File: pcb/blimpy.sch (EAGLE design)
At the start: 42 parts, among them IC1 TB6612FNG, J2 MICRO-USB, J3 JSTPH, Q1 mmbt2222, Q2 mmbt2222, Q3 DMG3415U, U1 RGB, U2 AP2112-3.3, U3 MCP73831T-2, U4 BNO080, U7 CP2104, U9 ESP-WROOM-32

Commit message: updated board design
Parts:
- removed C11: 10uF, SparkFun-Capacitors:10UF-0603-6.3V-20%
- removed IC1: TB6612FNG, adafruit:TB6612FNG
- added C12, C14, C15, C16, C17, C18, C19, C21, C22, C24, C25, C27: 0.1uF, SparkFun-Capacitors:0.1UF-0603-25V-5%
- added C28, C29, C30, C31: 10uF, SparkFun-Capacitors:10UF-POLAR-EIA3216-16V-10%(TANT)
- added C9: 10uF, SparkFun-Capacitors:10UF-0603-6.3V-20%
- added CN1, CN2, CN3, CN4, CN5, CN6, CN7, CN8: (no value), adafruit:JST_2PIN-SMT-RA
- added HB1, HB2, HB3, HB4: TB6612FNG, adafruit:TB6612FNG
- added J1: JSTPH, microbuilder:CON_JST_PH_2PIN
- added U5, U6: SX1509, SparkFun-IC-Special-Function:SX1509
- R4: value 4.7k -> 2.0k; device SparkFun-Resistors:4.7KOHM-0603-1/10W-1% -> SparkFun-Resistors:2.0KOHM-0603-1/10W-5%
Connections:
- removed net N$20: IC1.AO2, IC1.AO2'
- removed net N$24: IC1.BO1, IC1.BO1'
- removed net VBAT: C11.1, C3.1, C5.1, IC1.VM1, IC1.VM2, IC1.VM3, J3.2, Q3.D, R1.2, U3.VBAT
- removed net VBUS: D1.A, D2.A, J2.VBUS, Q3.G, R12.2, U3.VDD, U7G$1.VBUS
- new net IO1_RST: U5.!RESET
- new net IO2_RST: U6.!RESET
- new net M1_DIR: U5.I/O[12], U6.I/O[12]
- new net M1_PWM: U5.I/O[13], U6.I/O[13]
- new net M2_DIR: U5.I/O[14], U6.I/O[14]
- new net M2_PWM: U5.I/O[15], U6.I/O[15]
- new net M3_DIR: U5.I/O[8], U6.I/O[8]
- new net M3_PWM: U5.I/O[9], U6.I/O[9]
- new net M4_DIR: U5.I/O[10], U6.I/O[10]
- new net M4_PWM: U5.I/O[11], U6.I/O[11]
- new net M5_DIR: U5.I/O[4], U6.I/O[4]
- new net M5_PWM: U5.I/O[5], U6.I/O[5]
- new net M6_DIR: U5.I/O[6], U6.I/O[6]
- new net M6_PWM: U5.I/O[7], U6.I/O[7]
- new net N$17: CN1.1, HB1.AO2, HB1.AO2'
- new net N$21: CN2.1, HB1.BO1, HB1.BO1'
- new net N$23: CN3.2, HB2.AO1, HB2.AO1'
- new net N$25: CN3.1, HB2.AO2, HB2.AO2'
- new net N$33: CN4.1, HB2.BO1, HB2.BO1'
- new net N$35: CN5.1, HB3.AO2, HB3.AO2'
- new net N$37: CN6.1, HB3.BO1, HB3.BO1'
- new net N$38: CN7.2, HB4.AO1, HB4.AO1'
- new net N$39: CN7.1, HB4.AO2, HB4.AO2'
- new net N$41: CN8.1, HB4.BO1, HB4.BO1'
- new net N$5: CN1.2, HB1.AO1, HB1.AO1'
- new net S1_SIG: U5.I/O[0], U6.I/O[0]
- new net S2_SIG: U5.I/O[1], U6.I/O[1]
- new net S3_SIG: U5.I/O[2], U6.I/O[2]
- new net S4_SIG: U5.I/O[3], U6.I/O[3]
- new net V_BATT: C19.1, C22.1, C25.1, C28.+, C29.+, C3.1, C30.+, C31.+, C5.1, HB1.VM1, HB1.VM2, HB1.VM3, HB2.VM1, HB2.VM2, HB2.VM3, HB3.VM1, HB3.VM2, HB3.VM3, HB4.VM1, HB4.VM2, HB4.VM3, J3.2, Q3.D, R1.2, U3.VBAT
- new net V_USB: C9.1, D1.A, D2.A, J2.VBUS, Q3.G, R12.2, U3.VDD, U7G$1.VBUS
- net 3.3V: now also C12.1, C14.1, C15.1, C16.1, C17.1, C18.1, C21.1, C24.1, C27.1, HB1.STBY, HB1.VCC, HB2.STBY, HB2.VCC, HB3.STBY, HB3.VCC, HB4.STBY, HB4.VCC, U5.VCC1, U5.VCC2, U5.VDDM, U6.ADDR0, U6.VCC1, U6.VCC2, U6.VDDM; no longer IC1.STBY, IC1.VCC
- net GND: now also C12.2, C14.2, C15.2, C16.2, C17.2, C18.2, C19.2, C21.2, C22.2, C24.2, C25.2, C27.2, C28.-, C29.-, C30.-, C31.-, C9.2, HB1.GND, HB1.PGND1, HB1.PGND1', HB1.PGND2, HB1.PGND2', HB2.GND, HB2.PGND1, HB2.PGND1', HB2.PGND2, HB2.PGND2', HB3.GND, HB3.PGND1, HB3.PGND1', HB3.PGND2, HB3.PGND2', HB4.GND, HB4.PGND1, HB4.PGND1', HB4.PGND2, HB4.PGND2', U5.ADDR0, U5.ADDR1, U5.GND, U6.ADDR1, U6.GND; no longer C11.2, IC1.GND, IC1.PGND1, IC1.PGND1', IC1.PGND2, IC1.PGND2'
- net N$18: now also CN5.2, HB3.AO1, HB3.AO1'; no longer IC1.AO1, IC1.AO1'
- net N$22: now also CN2.2, CN4.2, CN6.2, CN8.2, HB1.BO2, HB1.BO2', HB2.BO2, HB2.BO2', HB3.BO2, HB3.BO2', HB4.BO2, HB4.BO2'; no longer IC1.BO2, IC1.BO2'
- net N$26: now also HB1.PWMB, HB2.PWMB, HB3.PWMB, HB4.PWMB; no longer IC1.PWMB
- net N$27: now also HB1.BIN2, HB2.BIN2, HB3.BIN2, HB4.BIN2; no longer IC1.BIN2
- net N$28: now also HB1.BIN1, HB2.BIN1, HB3.BIN1, HB4.BIN1; no longer IC1.BIN1
- net N$30: now also HB1.AIN1, HB2.AIN1, HB3.AIN1, HB4.AIN1; no longer IC1.AIN1
- net N$31: now also HB1.AIN2, HB2.AIN2, HB3.AIN2, HB4.AIN2; no longer IC1.AIN2
- net N$32: now also HB1.PWMA, HB2.PWMA, HB3.PWMA, HB4.PWMA; no longer IC1.PWMA
- net SCL: now also U5.SCL, U6.SCL
- net SDA: now also U5.SDA, U6.SDA
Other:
- note added: "600mA (800mA max)"
- note added: "GPIO Expander 1 I2C Address: 0x3E"
- note added: "GPIO Expander 2 I2C Address: 0x3F"
- note added: "TODO - Connect IMU to MC - Connect IO1 and IO2 to MC - Servos - H-Bridges - Add. Battery - Expose unused GPIO - ESD Protection? - Capacitors"
- note added: "up to 500mA charging current"
- note removed: "up to 200mA charging current"
- moved on the sheet: C1, C10, C13, C2, C3, C4, C5, C6, C7, C8, D1, D2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

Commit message: updated
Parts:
- removed CN1, CN2, CN3, CN4, CN5, CN6, CN7, CN8: (no value), adafruit:JST_2PIN-SMT-RA
- removed J3: JSTPH, microbuilder:CON_JST_PH_2PIN
- added J10, J11, J12, J13, J14, J15, J8, J9: (no value), SparkFun-Connectors:CONN_02-JST-2MM-SMT
- added J4, J5, J6, J7: 3-PIN SMD, SparkFun-Connectors:CONN_03JST-SMD
- added JP1: JUMPER-SMT_2_NO_SILK, SparkFun-Jumpers:JUMPER-SMT_2_NO_SILK
- J1: value JSTPH -> MICRO-USB; device microbuilder:CON_JST_PH_2PIN -> SparkFun-Connectors:USB_MICRO-B_SMT
- J2: value MICRO-USB -> (none); device SparkFun-Connectors:USB_MICRO-B_SMT -> SparkFun-Connectors:CONN_02-JST-2MM-SMT
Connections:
- removed net M1_DIR: U5.I/O[12], U6.I/O[12]
- removed net M1_PWM: U5.I/O[13], U6.I/O[13]
- removed net M2_DIR: U5.I/O[14], U6.I/O[14]
- removed net M2_PWM: U5.I/O[15], U6.I/O[15]
- removed net M3_DIR: U5.I/O[8], U6.I/O[8]
- removed net M3_PWM: U5.I/O[9], U6.I/O[9]
- removed net M4_DIR: U5.I/O[10], U6.I/O[10]
- removed net M4_PWM: U5.I/O[11], U6.I/O[11]
- removed net M5_DIR: U5.I/O[4], U6.I/O[4]
- removed net M5_PWM: U5.I/O[5], U6.I/O[5]
- removed net M6_DIR: U5.I/O[6], U6.I/O[6]
- removed net M6_PWM: U5.I/O[7], U6.I/O[7]
- removed net N$26: HB1.PWMB, HB2.PWMB, HB3.PWMB, HB4.PWMB
- removed net N$27: HB1.BIN2, HB2.BIN2, HB3.BIN2, HB4.BIN2
- removed net N$28: HB1.BIN1, HB2.BIN1, HB3.BIN1, HB4.BIN1
- removed net N$30: HB1.AIN1, HB2.AIN1, HB3.AIN1, HB4.AIN1
- removed net N$31: HB1.AIN2, HB2.AIN2, HB3.AIN2, HB4.AIN2
- removed net N$32: HB1.PWMA, HB2.PWMA, HB3.PWMA, HB4.PWMA
- removed net S1_SIG: U5.I/O[0], U6.I/O[0]
- removed net S2_SIG: U5.I/O[1], U6.I/O[1]
- removed net S3_SIG: U5.I/O[2], U6.I/O[2]
- removed net S4_SIG: U5.I/O[3], U6.I/O[3]
- new net 1-1: U5.I/O[0]
- new net 1-10: U5.I/O[9]
- new net 1-11: U5.I/O[10]
- new net 1-12: U5.I/O[11]
- new net 1-13: U5.I/O[12]
- new net 1-14: U5.I/O[13]
- new net 1-15: U5.I/O[14]
- new net 1-16: U5.I/O[15]
- new net 1-2: U5.I/O[1]
- new net 1-3: U5.I/O[2]
- new net 1-4: U5.I/O[3]
- new net 1-5: U5.I/O[4]
- new net 1-6: U5.I/O[5]
- new net 1-7: U5.I/O[6]
- new net 1-8: U5.I/O[7]
- new net 1-9: U5.I/O[8]
- new net 2-1: U6.I/O[0]
- new net 2-10: U6.I/O[9]
- new net 2-11: U6.I/O[10]
- new net 2-12: U6.I/O[11]
- new net 2-13: U6.I/O[12]
- new net 2-14: U6.I/O[13]
- new net 2-15: U6.I/O[14]
- new net 2-16: U6.I/O[15]
- new net 2-2: U6.I/O[1]
- new net 2-3: U6.I/O[2]
- new net 2-4: U6.I/O[3]
- new net 2-5: U6.I/O[4]
- new net 2-6: U6.I/O[5]
- new net 2-7: U6.I/O[6]
- new net 2-8: U6.I/O[7]
- new net 2-9: U6.I/O[8]
- new net H1-1: HB1.PWMA
- new net H1-2: HB1.AIN2
- new net H1-3: HB1.AIN1
- new net H1-4: HB1.BIN1
- new net H1-5: HB1.BIN2
- new net H1-6: HB1.PWMB
- new net H2-1: HB2.PWMA
- new net H2-2: HB2.AIN2
- new net H2-3: HB2.AIN1
- new net H2-4: HB2.BIN1
- new net H2-5: HB2.BIN2
- new net H2-6: HB2.PWMB
- new net H3-1: HB3.PWMA
- new net H3-2: HB3.AIN2
- new net H3-3: HB3.AIN1
- new net H3-4: HB3.BIN1
- new net H3-5: HB3.BIN2
- new net H3-6: HB3.PWMB
- new net H4-1: HB4.PWMA
- new net H4-2: HB4.AIN2
- new net H4-3: HB4.AIN1
- new net H4-4: HB4.BIN1
- new net H4-5: HB4.BIN2
- new net H4-6: HB4.PWMB
- new net N$19: J4.3, J5.3, J6.3, J7.3
- net GND: now also J1.GND, J1.SHIELD, J2.2, J4.2, J5.2, J6.2, J7.2; no longer J2.GND, J2.SHIELD, J3.1
- net N$17: now also J8.1; no longer CN1.1
- net N$18: now also J12.2; no longer CN5.2
- net N$2: now also J1.D+; no longer J2.D+
- net N$21: now also J9.1; no longer CN2.1
- net N$22: now also J11.2, J13.2, J15.2, J9.2; no longer CN2.2, CN4.2, CN6.2, CN8.2
- net N$23: now also J10.2; no longer CN3.2
- net N$25: now also J10.1; no longer CN3.1
- net N$33: now also J11.1; no longer CN4.1
- net N$35: now also J12.1; no longer CN5.1
- net N$37: now also J13.1; no longer CN6.1
- net N$38: now also J14.2; no longer CN7.2
- net N$39: now also J14.1; no longer CN7.1
- net N$4: now also JP1.1
- net N$41: now also J15.1; no longer CN8.1
- net N$5: now also J8.2; no longer CN1.2
- net N$6: now also J1.D-; no longer J2.D-
- net V_BATT: now also J2.1, J4.1, J5.1, J6.1, J7.1; no longer J3.2
- net V_USB: now also J1.VBUS, JP1.2; no longer J2.VBUS
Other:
- note added: "BOARD POWER"
- note added: "MOTORS"
- note added: "SERVOS"
- note added: "TODO - Connect IMU to MC - Connect Servos to MC - Connect H-Bridges to IOs - Connect IOs to MC - Expose unused GPIOs - ESD Protection? - Capacitors - Check all components"
- note added: "up to 500mA charging current close jumper to disable"
- note removed: "POWER AND FILTERING"
- note removed: "TODO - Connect IMU to MC - Connect IO1 and IO2 to MC - Servos - H-Bridges - Add. Battery - Expose unused GPIO - ESD Protection? - Capacitors"
- note removed: "up to 500mA charging current"
- moved on the sheet: C13, C19, C21, C22, C24, C25, C27, C28, C29, C30, C31, C5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

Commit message: added battery gauge
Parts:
- removed R1, R3: 100k, SparkFun-Resistors:100KOHM-0603-1/10W-1%
- added C11: 0.1uF, SparkFun-Capacitors:0.1UF-0603-25V-5%
- added U10: MAX17048, SparkFun-IC-Power:MAX17048DFN8
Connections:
- removed net BAT: R1.1, R3.2, U9.34-IA
- net GND: now also C11.2, U10.CTG, U10.GND, U10.QSTRT; no longer R3.1
- net SCL: now also U10.SCL
- net SDA: now also U10.SDA
- net V_BATT: now also C11.1, U10.CELL, U10.VDD; no longer R1.2
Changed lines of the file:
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@@
 <part name="Q3" library="microbuilder" deviceset="MOSFET-P" device="" value="DMG3415U"/>
 <part name="R12" library="SparkFun-Resistors" deviceset="100KOHM" device="-0603-1/10W-1%" value="100k"/>
-<part name="R1" library="SparkFun-Resistors" deviceset="100KOHM" device="-0603-1/10W-1%" value="100k"/>
-<part name="R3" library="SparkFun-Resistors" deviceset="100KOHM" device="-0603-1/10W-1%" value="100k"/>
 <part name="R4" library="SparkFun-Resistors" library_urn="urn:adsk.eagle:library:532" deviceset="2.0KOHM" device="-0603-1/10W-5%" package3d_urn="urn:adsk.eagle:package:39650/1" value="2.0k"/>
 <part name="S1" library="SparkFun-Switches" deviceset="SWITCH-SPDT" device="-SMD-RIGHT-ANGLE" value="PWR"/>
@@
 <part name="J7" library="SparkFun-Connectors" library_urn="urn:adsk.eagle:library:513" deviceset="CONN_03" device="JST-SMD" package3d_urn="urn:adsk.eagle:package:38075/1" value="3-PIN SMD"/>
 <part name="JP1" library="SparkFun-Jumpers" library_urn="urn:adsk.eagle:library:528" deviceset="JUMPER-SMT_2_NO" device="_SILK" package3d_urn="urn:adsk.eagle:package:39279/1"/>
+<part name="U10" library="SparkFun-IC-Power" library_urn="urn:adsk.eagle:library:526" deviceset="MAX17048" device="DFN8" package3d_urn="urn:adsk.eagle:package:39085/1" value="MAX17048"/>
+<part name="C11" library="SparkFun-Capacitors" library_urn="urn:adsk.eagle:library:510" deviceset="0.1UF" device="-0603-25V-5%" package3d_urn="urn:adsk.eagle:package:37414/1" value="0.1uF"/>
 </parts>
 <sheets>
@@
 <text x="200.66" y="124.46" size="1.778" layer="94">PROGRAMMING</text>
 <text x="17.78" y="121.92" size="1.27" layer="97">CHARGING LED</text>
-<text x="93.98" y="121.92" size="1.27" layer="97">CHARGE
+<text x="121.92" y="127" size="1.27" layer="97">CHARGE
 MEASUREMENT</text>
 <text x="43.18" y="45.72" size="1.778" layer="94">I2C PULL-UP
@@
 I2C Address: 0x4A</text>
 <text x="378.46" y="185.42" size="1.27" layer="97">INT OSC</text>
-<text x="665.48" y="220.98" size="5.08" layer="94" align="top-left">TODO
+<text x="160.02" y="-58.42" size="5.08" layer="94" align="top-left">TODO
 - Connect IMU to MC
 - Connect Servos to MC
@@
 <attribute name="VALUE" x="29.464" y="182.88" size="1.778" layer="96" font="vector" rot="R90" align="top-center"/>
 </instance>
-<instance part="R1" gate="G$1" x="106.68" y="111.76" smashed="yes" rot="R90">
-<attribute name="NAME" x="105.156" y="111.76" size="1.778" layer="95" font="vector" rot="R90" align="bottom-center"/>
-<attribute name="VALUE" x="108.204" y="111.76" size="1.778" layer="96" font="vector" rot="R90" align="top-center"/>
-</instance>
-<instance part="R3" gate="G$1" x="106.68" y="96.52" smashed="yes" rot="R90">
-<attribute name="NAME" x="105.156" y="96.52" size="1.778" layer="95" font="vector" rot="R90" align="bottom-center"/>
-<attribute name="VALUE" x="108.204" y="96.52" size="1.778" layer="96" font="vector" rot="R90" align="top-center"/>
-</instance>
 <instance part="R4" gate="G$1" x="78.74" y="106.68" smashed="yes" rot="R90">
 <attribute name="NAME" x="77.216" y="106.68" size="1.778" layer="95" font="vector" rot="R90" align="bottom-center"/>
@@
 <instance part="JP1" gate="G$1" x="78.74" y="127" smashed="yes" rot="R90">
 <attribute name="NAME" x="76.2" y="124.46" size="1.778" layer="95" font="vector" rot="R90"/>
+</instance>
+<instance part="U10" gate="G$1" x="132.08" y="111.76" smashed="yes">
+<attribute name="NAME" x="121.92" y="122.428" size="1.778" layer="95" font="vector"/>
+<attribute name="VALUE" x="121.92" y="99.06" size="1.778" layer="96" font="vector"/>
+</instance>
+<instance part="C11" gate="G$1" x="106.68" y="106.68" smashed="yes">
+<attribute name="NAME" x="108.204" y="109.601" size="1.778" layer="95" font="vector"/>
+<attribute name="VALUE" x="108.204" y="104.521" size="1.778" layer="96" font="vector"/>
 </instance>
 </instances>
@@
 </segment>
 <segment>
-<pinref part="R3" gate="G$1" pin="1"/>
 <pinref part="U3" gate="G$1" pin="VSS"/>
-<wire x1="106.68" y1="88.9" x2="106.68" y2="91.44" width="0.1524" layer="91"/>
 <wire x1="68.58" y1="114.3" x2="71.12" y2="114.3" width="0.1524" layer="91"/>
 <wire x1="71.12" y1="114.3" x2="71.12" y2="96.52" width="0.1524" layer="91"/>
@@
 <wire x1="35.56" y1="96.52" x2="71.12" y2="96.52" width="0.1524" layer="91"/>
 <junction x="71.12" y="96.52"/>
-<wire x1="106.68" y1="88.9" x2="88.9" y2="88.9" width="0.1524" layer="91"/>
-<wire x1="88.9" y1="88.9" x2="88.9" y2="96.52" width="0.1524" layer="91"/>
-<junction x="88.9" y="96.52"/>
 <wire x1="78.74" y1="101.6" x2="78.74" y2="96.52" width="0.1524" layer="91"/>
 <junction x="78.74" y="96.52"/>
 <pinref part="GND12" gate="1" pin="GND"/>
 <wire x1="71.12" y1="88.9" x2="71.12" y2="96.52" width="0.1524" layer="91"/>
+<pinref part="U10" gate="G$1" pin="QSTRT"/>
+<wire x1="142.24" y1="104.14" x2="144.78" y2="104.14" width="0.1524" layer="91"/>
+<wire x1="144.78" y1="104.14" x2="144.78" y2="96.52" width="0.1524" layer="91"/>
+<pinref part="U10" gate="G$1" pin="CTG"/>
+<wire x1="119.38" y1="109.22" x2="116.84" y2="109.22" width="0.1524" layer="91"/>
+<pinref part="U10" gate="G$1" pin="GND"/>
+<wire x1="119.38" y1="104.14" x2="116.84" y2="104.14" width="0.1524" layer="91"/>
+<wire x1="116.84" y1="109.22" x2="116.84" y2="104.14" width="0.1524" layer="91"/>
+<wire x1="116.84" y1="104.14" x2="116.84" y2="96.52" width="0.1524" layer="91"/>
+<junction x="116.84" y="104.14"/>
+<wire x1="144.78" y1="96.52" x2="116.84" y2="96.52" width="0.1524" layer="91"/>
+<junction x="116.84" y="96.52"/>
+<wire x1="88.9" y1="96.52" x2="106.68" y2="96.52" width="0.1524" layer="91"/>
+<junction x="88.9" y="96.52"/>
+<pinref part="C11" gate="G$1" pin="2"/>
+<wire x1="106.68" y1="96.52" x2="116.84" y2="96.52" width="0.1524" layer="91"/>
+<wire x1="106.68" y1="104.14" x2="106.68" y2="96.52" width="0.1524" layer="91"/>
+<junction x="106.68" y="96.52"/>
 </segment>
 <segment>
@@
 </segment>
 </net>
-<net name="BAT" class="0">
-<segment>
-<pinref part="R1" gate="G$1" pin="1"/>
-<pinref part="R3" gate="G$1" pin="2"/>
-<label x="111.76" y="104.14" size="1.27" layer="95" xref="yes"/>
-<wire x1="106.68" y1="101.6" x2="106.68" y2="104.14" width="0.1524" layer="91"/>
-<wire x1="106.68" y1="104.14" x2="106.68" y2="106.68" width="0.1524" layer="91"/>
-<wire x1="106.68" y1="104.14" x2="111.76" y2="104.14" width="0.1524" layer="91"/>
-<junction x="106.68" y="104.14"/>
-</segment>
-<segment>
-<pinref part="U9" gate="G$1" pin="34-IA"/>
-<wire x1="172.72" y1="17.78" x2="152.4" y2="17.78" width="0.1524" layer="91"/>
-<label x="152.4" y="17.78" size="1.27" layer="95" rot="R180" xref="yes"/>
-</segment>
-</net>
 <net name="RED" class="0">
 <segment>
@@
 <label x="322.58" y="-35.56" size="1.27" layer="95" rot="R180" xref="yes"/>
 </segment>
+<segment>
+<pinref part="U10" gate="G$1" pin="SDA"/>
+<wire x1="142.24" y1="114.3" x2="144.78" y2="114.3" width="0.1524" layer="91"/>
+<label x="144.78" y="114.3" size="1.27" layer="95" xref="yes"/>
+</segment>
 </net>
 <net name="SCL" class="0">
@@
 <wire x1="322.58" y1="-38.1" x2="345.44" y2="-38.1" width="0.1524" layer="91"/>
 <label x="322.58" y="-38.1" size="1.27" layer="95" rot="R180" xref="yes"/>
+</segment>
+<segment>
+<pinref part="U10" gate="G$1" pin="SCL"/>
+<wire x1="142.24" y1="109.22" x2="144.78" y2="109.22" width="0.1524" layer="91"/>
+<label x="144.78" y="109.22" size="1.27" layer="95" xref="yes"/>
 </segment>
 </net>
@@
 <pinref part="U3" gate="G$1" pin="VBAT"/>
 <wire x1="68.58" y1="119.38" x2="88.9" y2="119.38" width="0.1524" layer="91"/>
+<junction x="88.9" y="119.38"/>
+<pinref part="SUPPLY6" gate="G$1" pin="V_BATT"/>
+<pinref part="U10" gate="G$1" pin="CELL"/>
+<wire x1="119.38" y1="114.3" x2="116.84" y2="114.3" width="0.1524" layer="91"/>
+<pinref part="U10" gate="G$1" pin="VDD"/>
+<wire x1="119.38" y1="119.38" x2="116.84" y2="119.38" width="0.1524" layer="91"/>
+<wire x1="116.84" y1="114.3" x2="116.84" y2="119.38" width="0.1524" layer="91"/>
+<junction x="116.84" y="119.38"/>
 <wire x1="88.9" y1="119.38" x2="106.68" y2="119.38" width="0.1524" layer="91"/>
-<junction x="88.9" y="119.38"/>
-<pinref part="R1" gate="G$1" pin="2"/>
-<wire x1="106.68" y1="116.84" x2="106.68" y2="119.38" width="0.1524" layer="91"/>
-<pinref part="SUPPLY6" gate="G$1" pin="V_BATT"/>
-</segment>
-<segment>
+<pinref part="C11" gate="G$1" pin="1"/>
+<wire x1="106.68" y1="119.38" x2="116.84" y2="119.38" width="0.1524" layer="91"/>
+<wire x1="106.68" y1="111.76" x2="106.68" y2="119.38" width="0.1524" layer="91"/>
+<junction x="106.68" y="119.38"/>
+</segment>
+<segment>

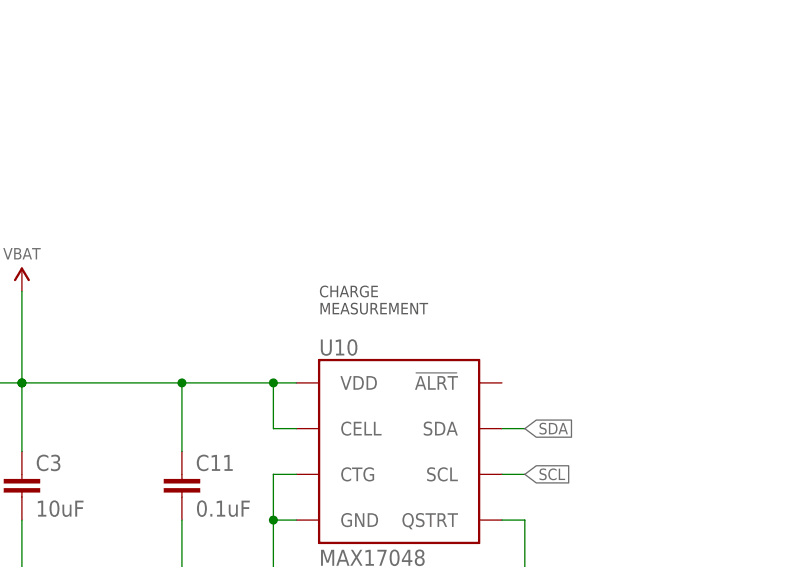
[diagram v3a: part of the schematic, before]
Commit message: added address
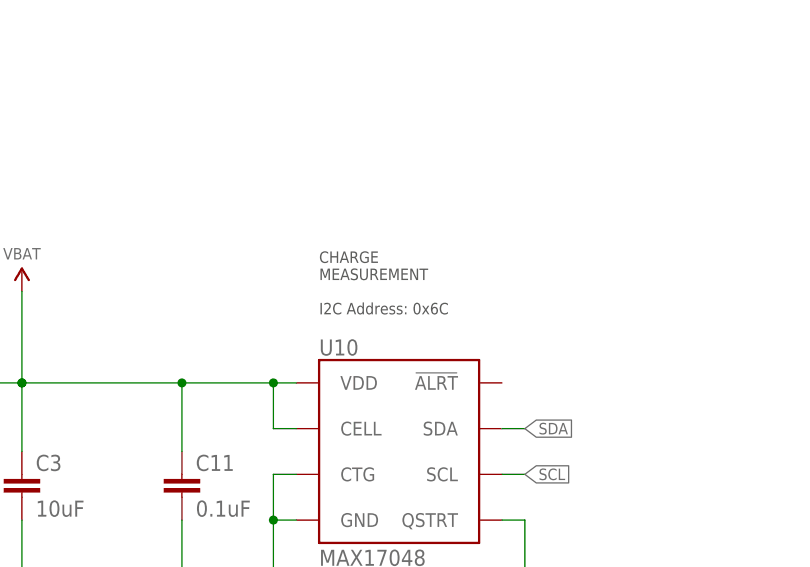
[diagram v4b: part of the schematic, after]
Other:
- note added: "CHARGE MEASUREMENT I2C Address: 0x6C"
- note removed: "CHARGE MEASUREMENT"
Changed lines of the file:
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@@
 <text x="17.78" y="121.92" size="1.27" layer="97">CHARGING LED</text>
 <text x="121.92" y="127" size="1.27" layer="97">CHARGE
-MEASUREMENT</text>
+MEASUREMENT
+I2C Address: 0x6C</text>
 <text x="43.18" y="45.72" size="1.778" layer="94">I2C PULL-UP
 RESISTORS</text>

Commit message: updated
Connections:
- removed net N$17: HB1.AO2, HB1.AO2', J8.1
- removed net N$18: HB3.AO1, HB3.AO1', J12.2
- removed net N$21: HB1.BO1, HB1.BO1', J9.1
- removed net N$22: HB1.BO2, HB1.BO2', HB2.BO2, HB2.BO2', HB3.BO2, HB3.BO2', HB4.BO2, HB4.BO2', J11.2, J13.2, J15.2, J9.2
- removed net N$23: HB2.AO1, HB2.AO1', J10.2
- removed net N$25: HB2.AO2, HB2.AO2', J10.1
- removed net N$33: HB2.BO1, HB2.BO1', J11.1
- removed net N$35: HB3.AO2, HB3.AO2', J12.1
- removed net N$37: HB3.BO1, HB3.BO1', J13.1
- removed net N$38: HB4.AO1, HB4.AO1', J14.2
- removed net N$39: HB4.AO2, HB4.AO2', J14.1
- removed net N$41: HB4.BO1, HB4.BO1', J15.1
- removed net N$5: HB1.AO1, HB1.AO1', J8.2
- new net HB1-A1: HB1.AO1, HB1.AO1', J8.1
- new net HB1-A2: HB1.AO2, HB1.AO2', J8.2
- new net HB1-B1: HB1.BO1, HB1.BO1', J9.2
- new net HB1-B2: HB1.BO2, HB1.BO2', J9.1
- new net HB2-A1: HB2.AO1, HB2.AO1', J10.1
- new net HB2-A2: HB2.AO2, HB2.AO2', J10.2
- new net HB2-B1: HB2.BO1, HB2.BO1', J11.2
- new net HB2-B2: HB2.BO2, HB2.BO2', J11.1
- new net HB3-A1: HB3.AO1, HB3.AO1', J12.1
- new net HB3-A2: HB3.AO2, HB3.AO2', J12.2
- new net HB3-B1: HB3.BO1, HB3.BO1', J13.2
- new net HB3-B2: HB3.BO2, HB3.BO2', J13.1
- new net HB4-A1: HB4.AO1, HB4.AO1', J14.1
- new net HB4-A2: HB4.AO2, HB4.AO2', J14.2
- new net HB4-B1: HB4.BO1, HB4.BO1', J15.2
- new net HB4-B2: HB4.BO2, HB4.BO2', J15.1
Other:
- note added: "TODO - Connect IMU to MC - Connect Servos to MC - Connect H-Bridges to IOs - Connect IOs to MC - Expose unused GPIOs - Add. Capacitors? - Check all components"
- note removed: "TODO - Connect IMU to MC - Connect Servos to MC - Connect H-Bridges to IOs - Connect IOs to MC - Expose unused GPIOs - ESD Protection? - Capacitors - Check all components"

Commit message: removed todo
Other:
- note added: "TODO - Connect IMU to MC - Connect Servos to MC - Connect H-Bridges to IOs - Connect IOs to MC - Expose unused GPIOs - Check all components"
- note removed: "TODO - Connect IMU to MC - Connect Servos to MC - Connect H-Bridges to IOs - Connect IOs to MC - Expose unused GPIOs - Add. Capacitors? - Check all components"
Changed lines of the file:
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@@
 - Connect IOs to MC
 - Expose unused GPIOs
-- Add. Capacitors?
 - Check all components</text>
 <text x="342.9" y="106.68" size="1.778" layer="94">GPIO Expander 1
